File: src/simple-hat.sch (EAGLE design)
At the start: 36 parts

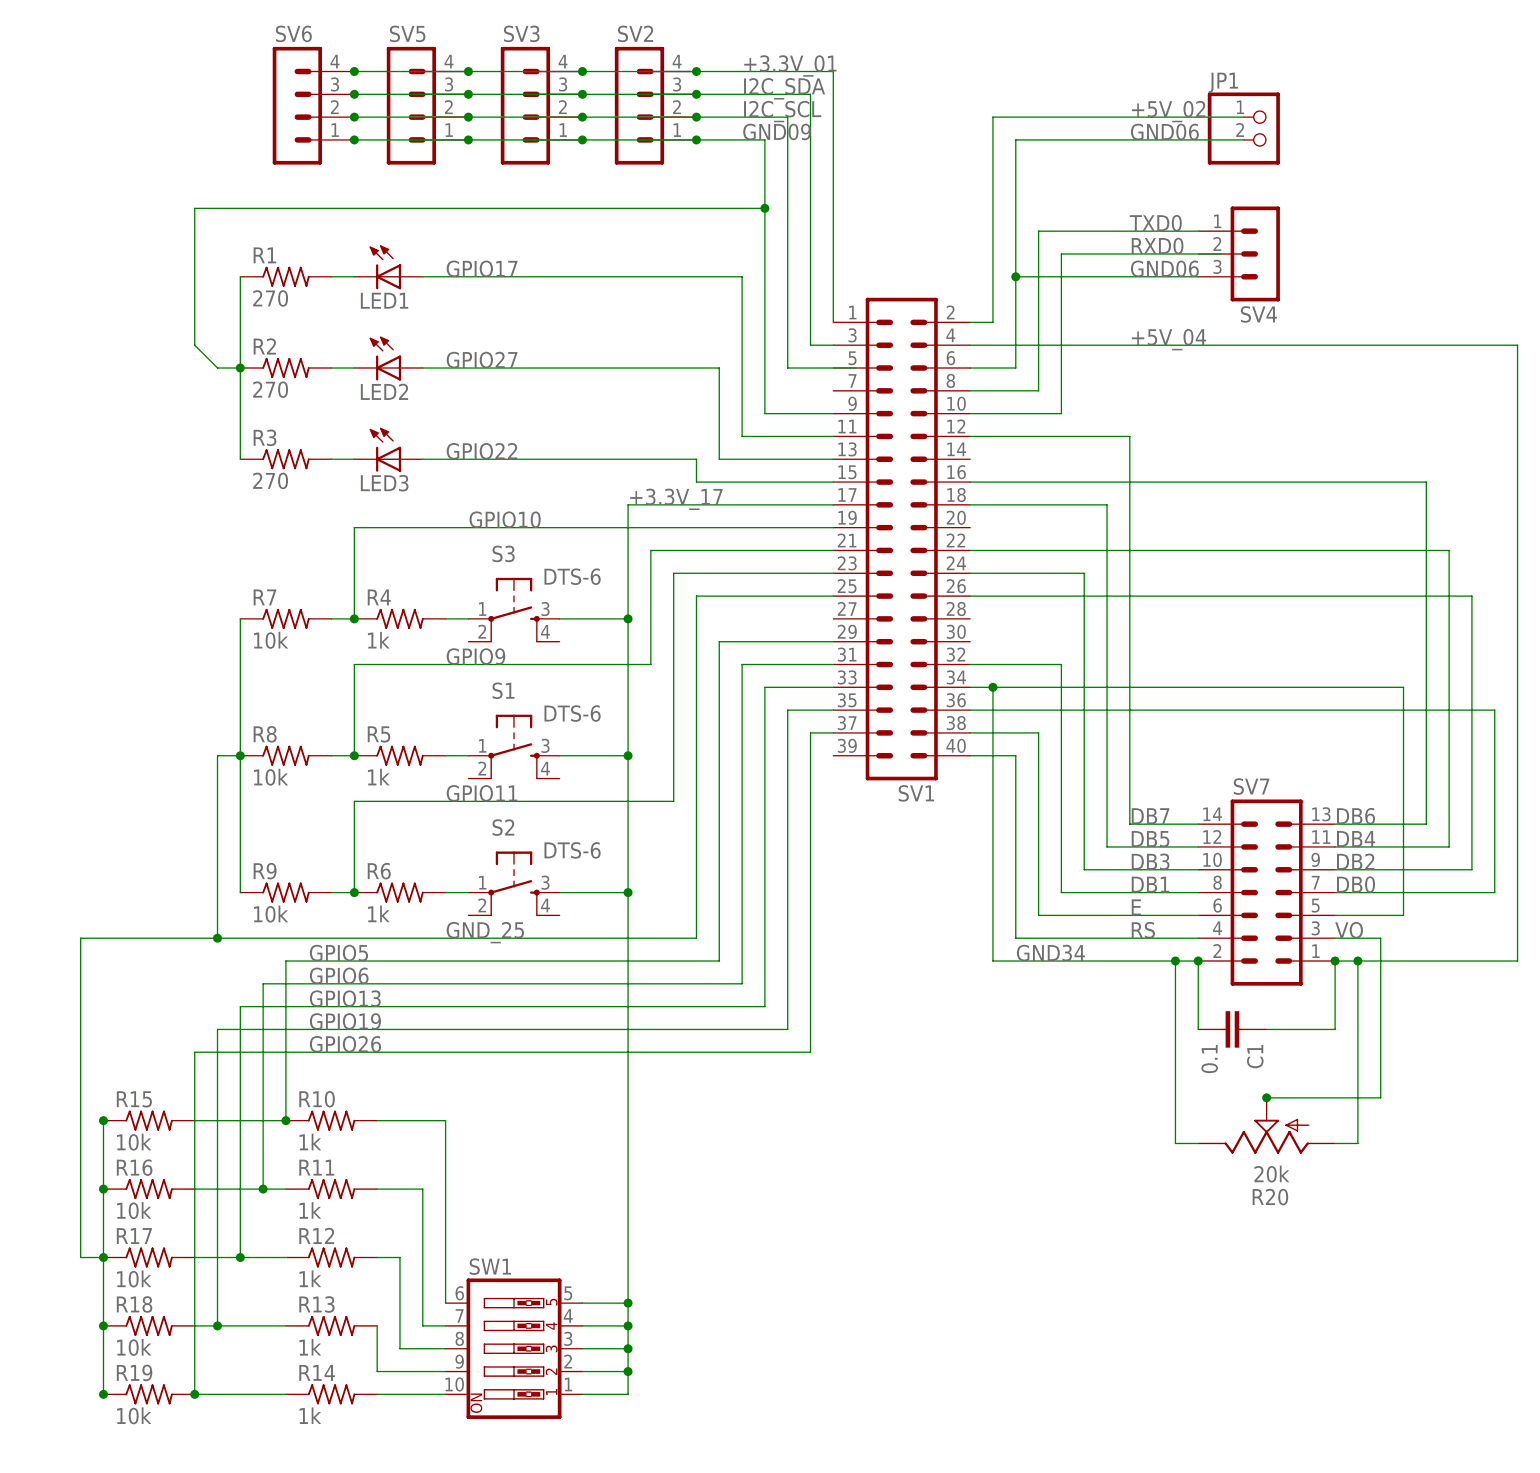
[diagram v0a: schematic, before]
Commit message: Added routed borad data
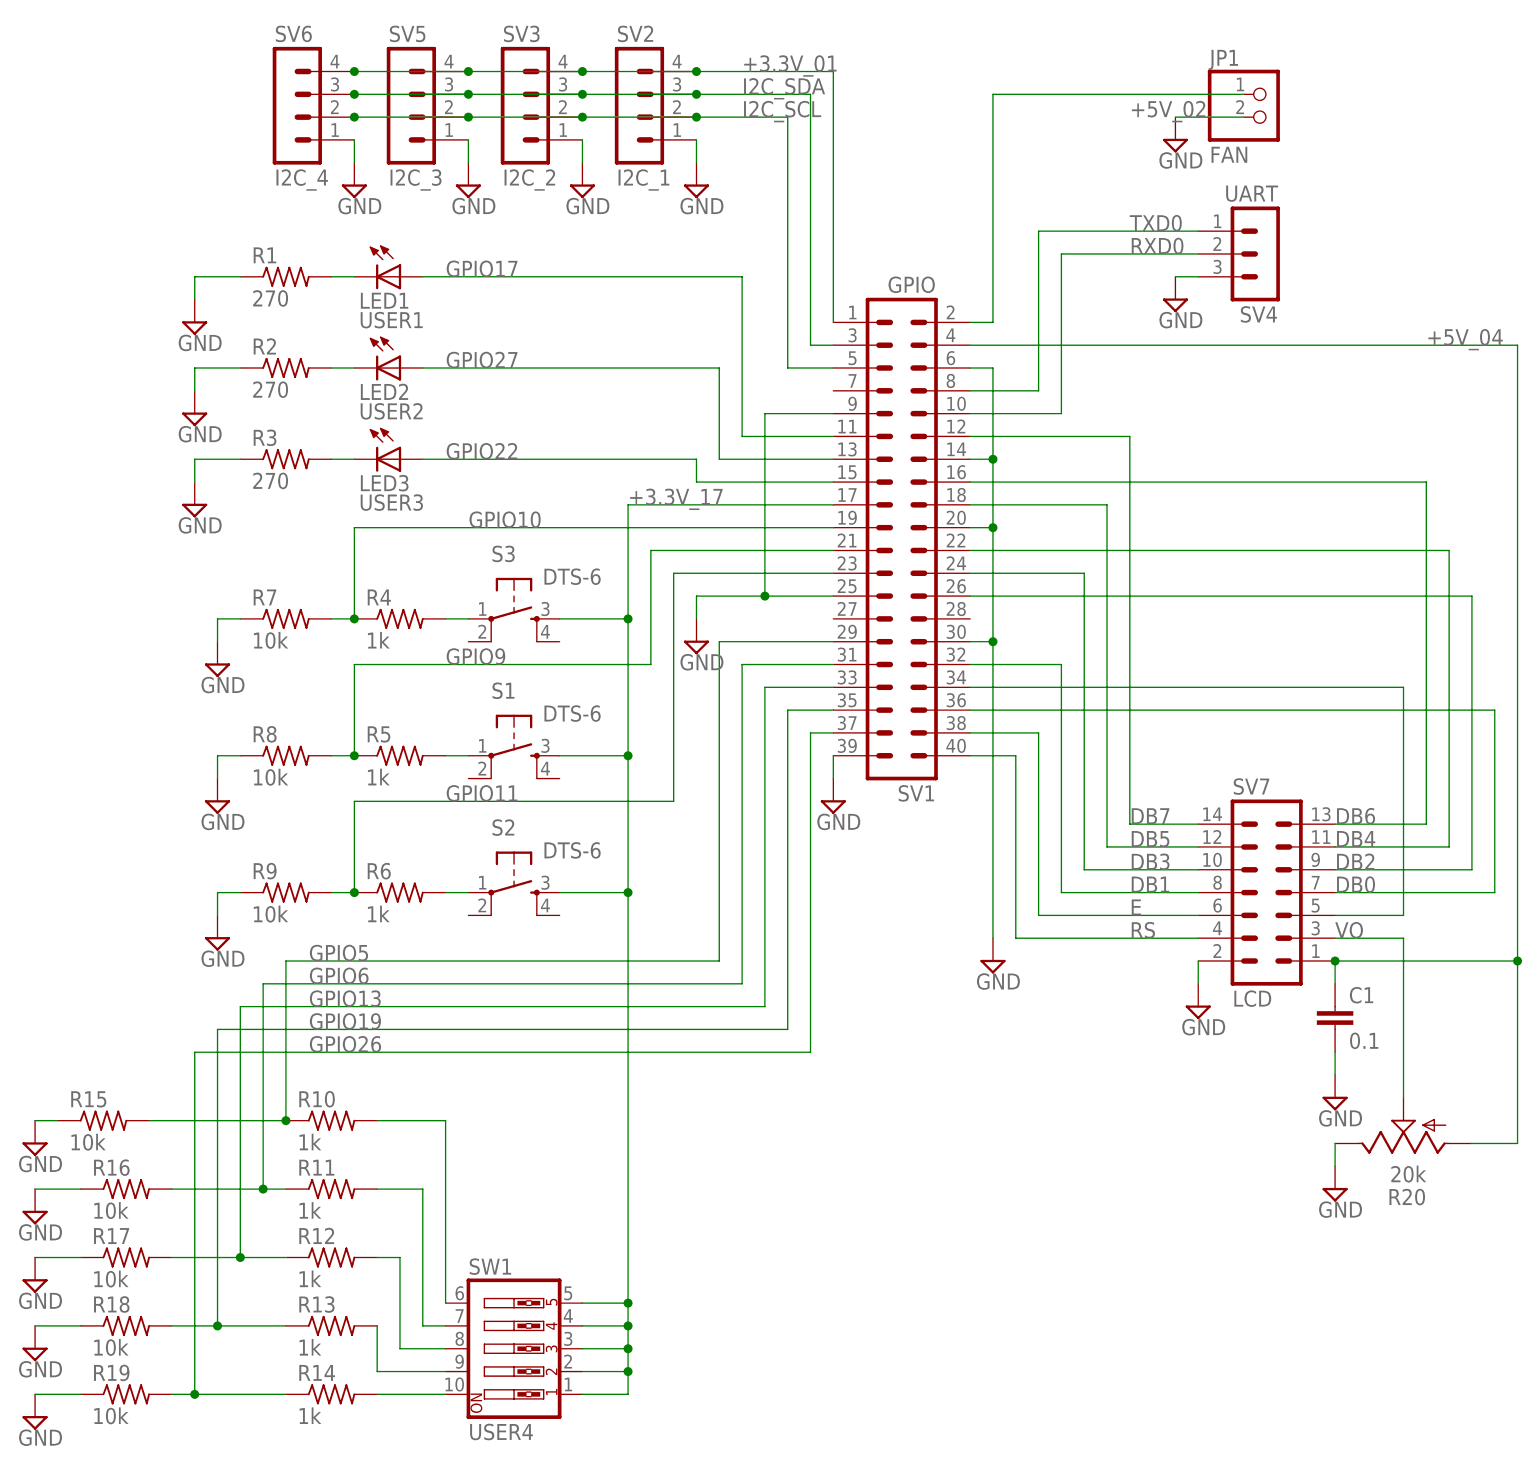
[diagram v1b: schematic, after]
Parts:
- JP1: value (none) -> FAN
- LED1: value (none) -> USER1
- LED2: value (none) -> USER2
- LED3: value (none) -> USER3
- SV1: value (none) -> GPIO
- SV2: value (none) -> I2C_1
- SV3: value (none) -> I2C_2
- SV4: value (none) -> UART
- SV5: value (none) -> I2C_3
- SV6: value (none) -> I2C_4
- SV7: value (none) -> LCD
- SW1: value (none) -> USER4
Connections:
- removed net GND06: JP1.2, SV1.6, SV4.3
- removed net GND09: R1.1, R2.1, R3.1, SV1.9, SV2.1, SV3.1, SV5.1, SV6.1
- removed net GND_25: R15.1, R16.1, R17.1, R18.1, R19.1, R7.1, R8.1, R9.1, SV1.25
- new net GND: C1.2, JP1.2, R1.1, R15.1, R16.1, R17.1, R18.1, R19.1, R2.1, R20.E, R3.1, R7.1, R8.1, R9.1, SV1.14, SV1.20, SV1.25, SV1.30, SV1.39, SV1.6, SV1.9, SV2.1, SV3.1, SV4.3, SV5.1, SV6.1, SV7.2
- net GND34: no longer C1.2, R20.E, SV7.2
- net I2C_SCL: now also SV1.5
- net RXD0: now also SV4.2
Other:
- moved on the sheet: C1, JP1, R15, R16, R17, R18, R19, R20
